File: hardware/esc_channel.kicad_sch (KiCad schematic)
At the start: 17 parts, among them Q32 AGM210MAP, Q33 AGM210MAP, Q34 AGM210MAP, U7 EFM8BB51F16I

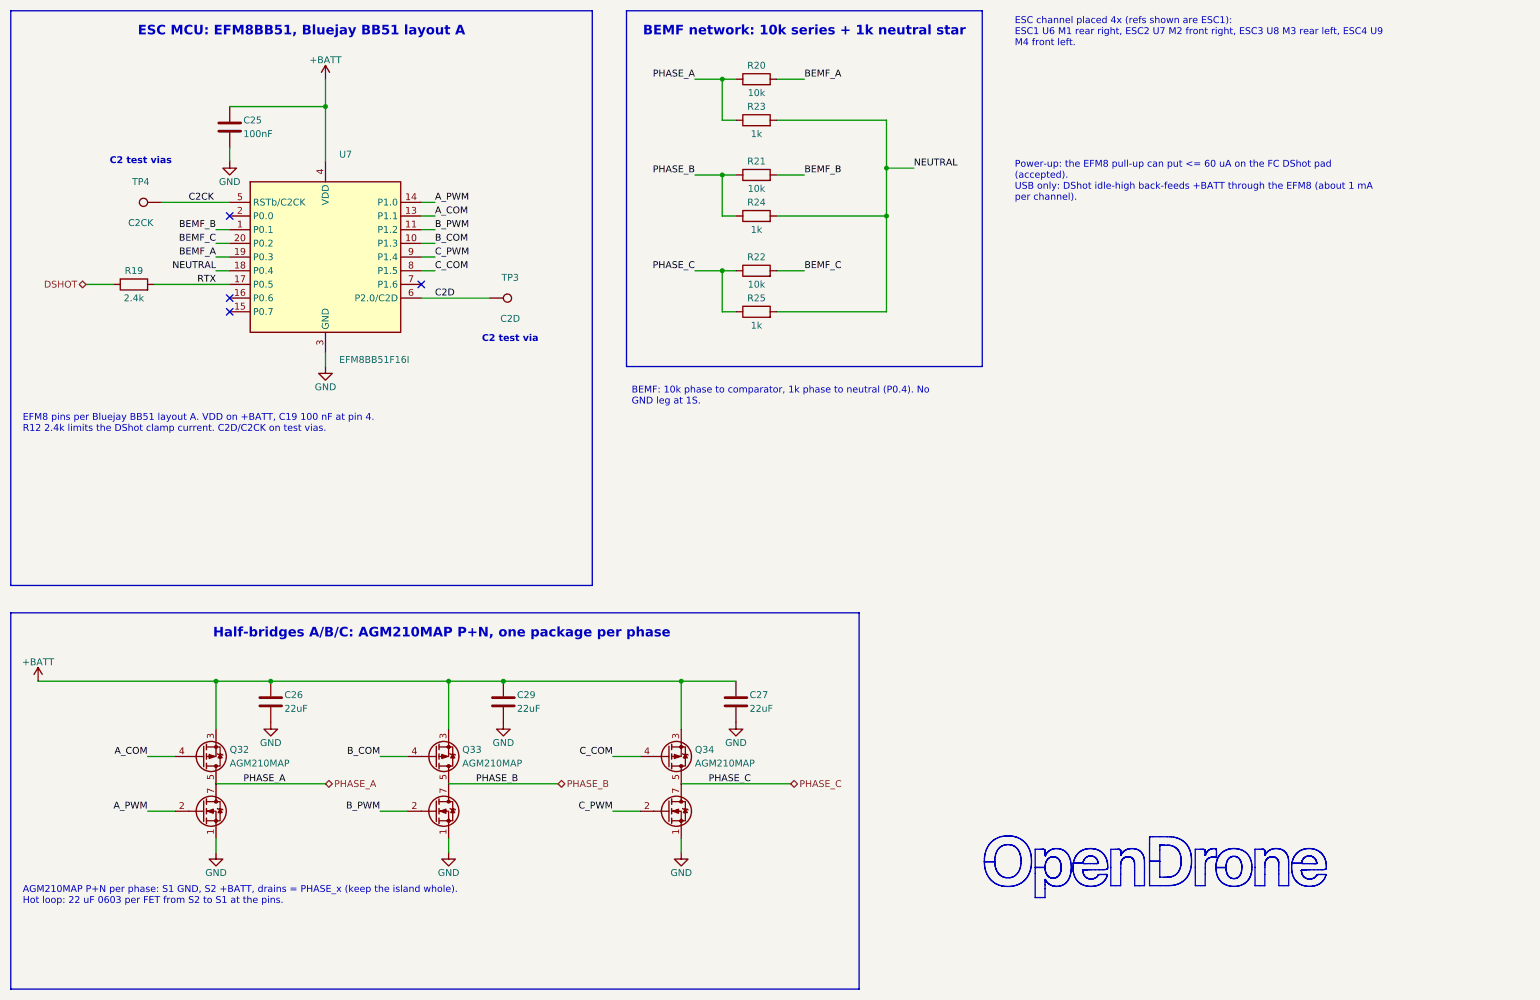
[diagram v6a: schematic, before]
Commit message: WIP placement and schematic snapshot for shared routing
Owner placement and schematic edits, firmware bindings, routing notes and
board tooling, so others can try the routing. Not DRC-clean; PCB not yet
updated from the schematic (R1 to R2, C1/C2/C134 removal).

Co-Authored-By: Claude Opus 5.5 <noreply@anthropic.com>
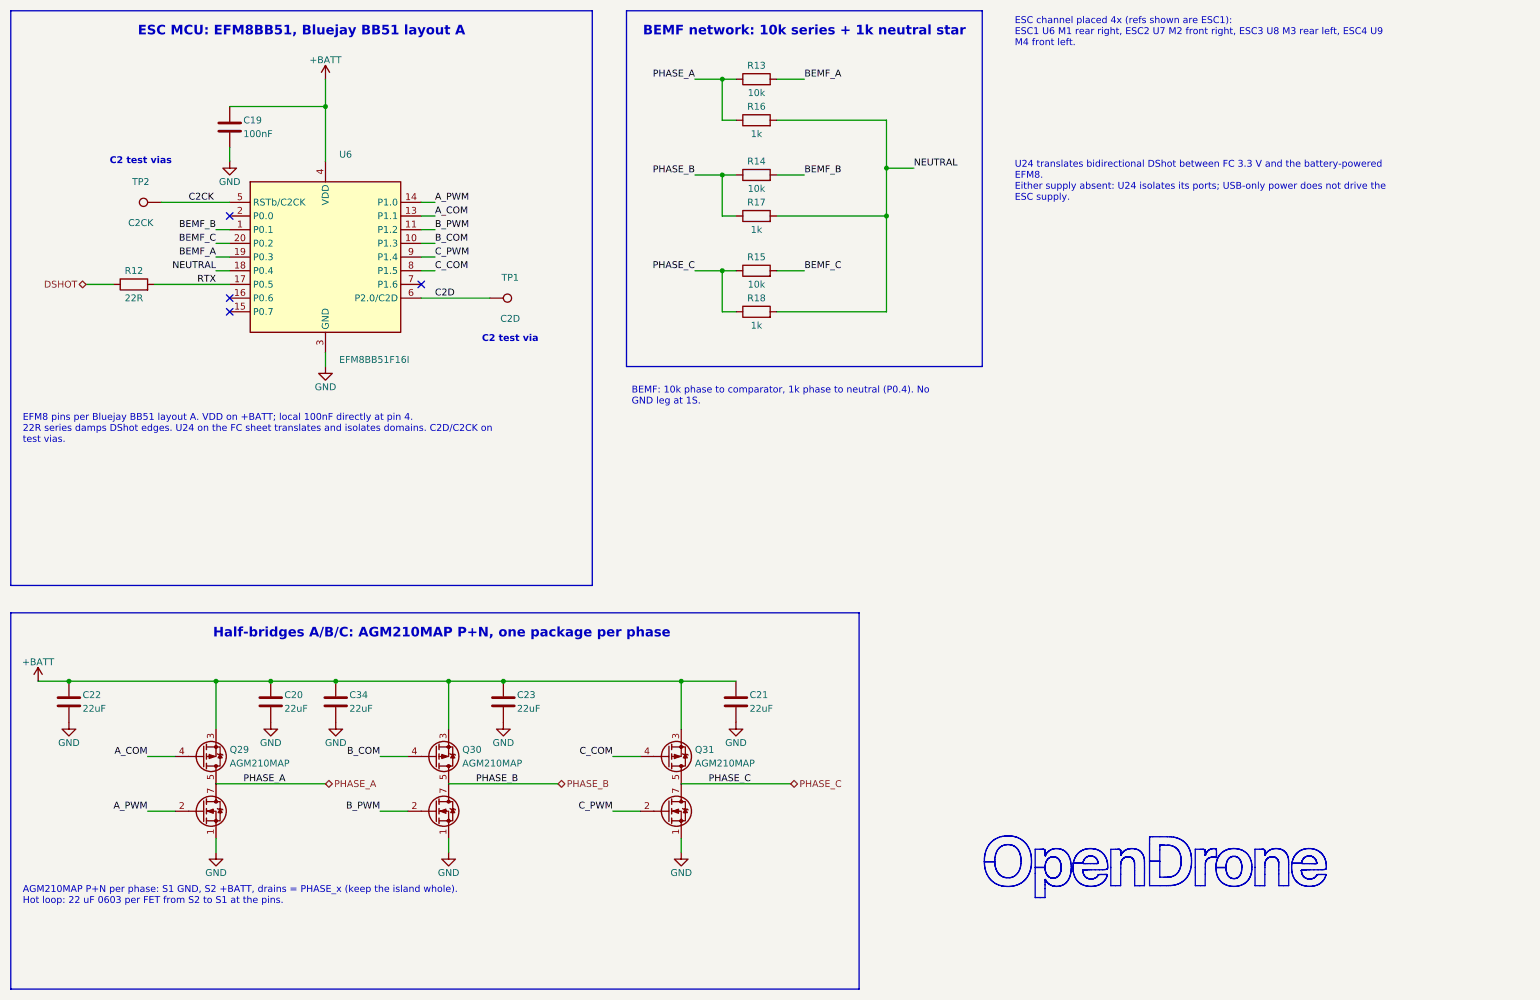
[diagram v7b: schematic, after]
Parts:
- added C22, C34: 22uF, lib:C_0603_1608Metric_L, symbol Device:C
- R12: renamed from R19; value 2.4k -> 22R; LCSC C166281 -> C155743; MPN RTT012401FTH -> RC0201FR-0722RL; Manufacturer Ralec -> Yageo
- renumbered C25 to C19, C26 to C20, C27 to C21, C29 to C23, Q32 to Q29, Q33 to Q30, Q34 to Q31, R20 to R13, R21 to R14, R22 to R15, R23 to R16, R24 to R17, R25 to R18, TP3 to TP1, TP4 to TP2, U7 to U6
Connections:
- net +BATT: now also C22.1, C34.1
- net GND: now also C22.2, C34.2

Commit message: WIP placement and schematic state before the 8L HDI change
Owner's uncommitted KiCad edits of 2026-10-12, committed as-is.

Co-Authored-By: Claude Opus 5.5 <noreply@anthropic.com>
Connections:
- net B_COM: now also Q31.4 (G2); no longer Q30.4 (G2)
- net B_PWM: now also Q31.2 (G1); no longer Q30.2 (G1)
- net C_COM: now also Q30.4 (G2); no longer Q31.4 (G2)
- net C_PWM: now also Q30.2 (G1); no longer Q31.2 (G1)
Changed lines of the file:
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@@
 	)
 	(label "C_PWM"
-		(at 129.54 163.83 180)
-		(effects
-			(font
-				(size 1.27 1.27)
-			)
-			(justify right bottom)
-		)
-	)
-	(label "B_PWM"
 		(at 86.36 163.83 180)
 		(effects
@@
 			)
 			(justify left bottom)
-		)
-	)
-	(label "C_COM"
-		(at 129.54 153.67 180)
-		(effects
-			(font
-				(size 1.27 1.27)
-			)
-			(justify right bottom)
 		)
 	)
@@
 		)
 	)
-	(label "B_COM"
+	(label "C_COM"
 		(at 86.36 153.67 180)
 		(effects
@@
 		)
 	)
+	(label "B_COM"
+		(at 129.54 153.67 180)
+		(effects
+			(font
+				(size 1.27 1.27)
+			)
+			(justify right bottom)
+		)
+	)
+	(label "B_PWM"
+		(at 129.54 163.83 180)
+		(effects
+			(font
+				(size 1.27 1.27)
+			)
+			(justify right bottom)
+		)
+	)
